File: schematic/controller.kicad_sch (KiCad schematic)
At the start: 2 parts, among them J5 Player 1, J7 Player 2

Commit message: bootup works, controller waits, but no response
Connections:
- net C2P4 is gone; now on net C4_ARM: J7.5
- net C2P7 is gone; now on net C7_FIRE: J7.8
- net C1P4 renamed C4_ARM
- net C1P7 renamed C7_FIRE
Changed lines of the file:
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@@
 (kicad_sch (version 20230121) (generator eeschema)
   (paper "A4")
-  (bus_entry (at 152.781 127.127) (size 2.54 2.54)
-    (stroke (width 0) (type default))
+  (junction (at 149.225 109.601) (diameter 0) (color 0 0 0 0)
+  )
+  (junction (at 151.13 112.649) (diameter 0) (color 0 0 0 0)
   )
   (bus_entry (at 152.781 84.709) (size 2.54 2.54)
@@
     (stroke (width 0) (type default))
   )
-  (bus_entry (at 152.781 134.747) (size 2.54 2.54)
-    (stroke (width 0) (type default))
-  )
   (bus_entry (at 152.781 124.587) (size 2.54 2.54)
     (stroke (width 0) (type default))
@@
     (stroke (width 0) (type default))
   )
-  (bus_entry (at 152.781 94.869) (size 2.54 2.54)
-    (stroke (width 0) (type default))
-  )
   (bus_entry (at 152.781 97.409) (size 2.54 2.54)
     (stroke (width 0) (type default))
@@
     (stroke (width 0) (type default))
   )
-  (bus_entry (at 152.781 102.489) (size 2.54 2.54)
-    (stroke (width 0) (type default))
-  )
   (bus_entry (at 152.781 132.207) (size 2.54 2.54)
     (stroke (width 0) (type default))
@@
     (stroke (width 0) (type default))
   )
-  (wire (pts (xy 141.859 127.127) (xy 152.781 127.127))
-    (stroke (width 0) (type default))
-  )
-  (wire (pts (xy 141.859 102.489) (xy 152.781 102.489))
+  (wire (pts (xy 141.859 102.489) (xy 151.13 102.489))
     (stroke (width 0) (type default))
   )
@@
     (stroke (width 0) (type default))
   )
+  (wire (pts (xy 141.859 127.127) (xy 149.225 127.127))
+    (stroke (width 0) (type default))
+  )
   (bus (pts (xy 155.321 87.249) (xy 155.321 89.789))
     (stroke (width 0) (type default))
@@
     (stroke (width 0) (type default))
   )
+  (wire (pts (xy 149.225 109.601) (xy 149.225 94.869))
+    (stroke (width 0) (type default))
+  )
   (bus (pts (xy 155.321 94.869) (xy 155.321 97.409))
     (stroke (width 0) (type default))
   )
-  (wire (pts (xy 141.859 134.747) (xy 152.781 134.747))
+  (wire (pts (xy 149.225 127.127) (xy 149.225 109.601))
     (stroke (width 0) (type default))
   )
@@
     (stroke (width 0) (type default))
   )
-  (bus (pts (xy 155.321 127.127) (xy 155.321 129.667))
+  (wire (pts (xy 151.13 102.489) (xy 151.13 112.649))
+    (stroke (width 0) (type default))
+  )
+  (wire (pts (xy 149.225 109.601) (xy 153.67 109.601))
     (stroke (width 0) (type default))
   )
@@
     (stroke (width 0) (type default))
   )
-  (wire (pts (xy 141.859 94.869) (xy 152.781 94.869))
+  (wire (pts (xy 151.13 112.649) (xy 151.13 134.747))
+    (stroke (width 0) (type default))
+  )
+  (wire (pts (xy 141.859 94.869) (xy 149.225 94.869))
     (stroke (width 0) (type default))
   )
@@
     (stroke (width 0) (type default))
   )
-  (bus (pts (xy 155.321 129.667) (xy 155.321 132.207))
+  (bus (pts (xy 155.321 127.127) (xy 155.321 132.207))
     (stroke (width 0) (type default))
   )
@@
     (stroke (width 0) (type default))
   )
+  (wire (pts (xy 141.859 134.747) (xy 151.13 134.747))
+    (stroke (width 0) (type default))
+  )
+  (wire (pts (xy 151.13 112.649) (xy 153.67 112.649))
+    (stroke (width 0) (type default))
+  )
   (label "C1P3" (at 141.986 97.409 0) (fields_autoplaced)
     (effects (font (size 1.27 1.27)) (justify left bottom))
@@
     (effects (font (size 1.27 1.27)) (justify left bottom))
   )
-  (label "C2P4" (at 141.986 134.747 0) (fields_autoplaced)
-    (effects (font (size 1.27 1.27)) (justify left bottom))
-  )
   (label "C1P0" (at 141.986 82.169 0) (fields_autoplaced)
     (effects (font (size 1.27 1.27)) (justify left bottom))
   )
-  (label "C1P4" (at 141.986 102.489 0) (fields_autoplaced)
-    (effects (font (size 1.27 1.27)) (justify left bottom))
-  )
   (label "C2P2" (at 141.986 124.587 0) (fields_autoplaced)
     (effects (font (size 1.27 1.27)) (justify left bottom))
@@
     (effects (font (size 1.27 1.27)) (justify left bottom))
   )
-  (label "C2P7" (at 142.113 127.127 0) (fields_autoplaced)
-    (effects (font (size 1.27 1.27)) (justify left bottom))
-  )
   (label "C1P5" (at 142.113 84.709 0) (fields_autoplaced)
     (effects (font (size 1.27 1.27)) (justify left bottom))
@@
     (effects (font (size 1.27 1.27)) (justify left bottom))
   )
-  (label "C1P7" (at 142.113 94.869 0) (fields_autoplaced)
-    (effects (font (size 1.27 1.27)) (justify left bottom))
-  )
   (label "C2P6" (at 142.113 122.047 0) (fields_autoplaced)
     (effects (font (size 1.27 1.27)) (justify left bottom))
@@
     (effects (font (size 1.27 1.27)) (justify left))
   )
+  (hierarchical_label "C7_FIRE" (shape input) (at 153.67 109.601 0) (fields_autoplaced)
+    (effects (font (size 1.27 1.27)) (justify left))
+  )
   (hierarchical_label "C1P[0..8]" (shape bidirectional) (at 159.766 105.029 0) (fields_autoplaced)
     (effects (font (size 1.27 1.27)) (justify left))
   )
+  (hierarchical_label "C4_ARM" (shape input) (at 153.67 112.649 0) (fields_autoplaced)
+    (effects (font (size 1.27 1.27)) (justify left))
+  )

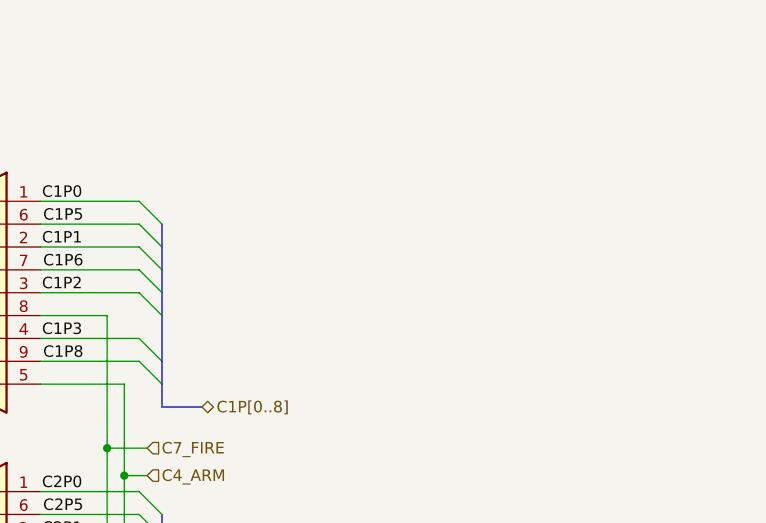
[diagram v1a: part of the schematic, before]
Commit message: added volume and adjusted cart port
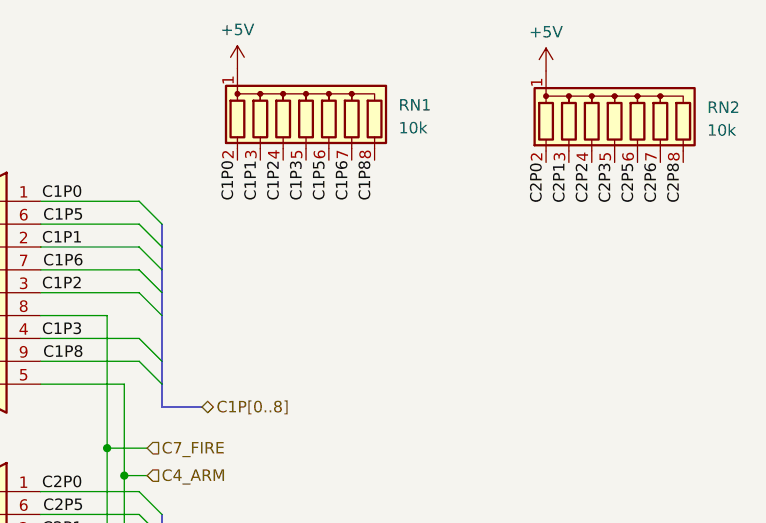
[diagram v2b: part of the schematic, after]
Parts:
- added RN1, RN2: 10k, Resistor_THT:R_Array_SIP8, symbol Device:R_Network07
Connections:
- net C1P0: now also RN1.2 (R1)
- net C1P1: now also RN1.3 (R2)
- net C1P2: now also RN1.4 (R3)
- net C1P3: now also RN1.5 (R4)
- net C1P5: now also RN1.6 (R5)
- net C1P6: now also RN1.7 (R6)
- net C1P8: now also RN1.8 (R7)
- net C2P0: now also RN2.2 (R1)
- net C2P1: now also RN2.3 (R2)
- net C2P2: now also RN2.4 (R3)
- net C2P3: now also RN2.5 (R4)
- net C2P5: now also RN2.6 (R5)
- net C2P6: now also RN2.7 (R6)
- net C2P8: now also RN2.8 (R7)
- new net +5V: RN1.1 (common), RN2.1 (common)
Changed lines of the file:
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@@
     (stroke (width 0) (type default))
   )
-  (bus (pts (xy 155.321 97.409) (xy 155.321 99.949))
+  (bus (pts (xy 155.321 94.869) (xy 155.321 99.949))
     (stroke (width 0) (type default))
   )
@@
     (stroke (width 0) (type default))
   )
-  (bus (pts (xy 155.321 94.869) (xy 155.321 97.409))
-    (stroke (width 0) (type default))
-  )
   (wire (pts (xy 149.225 127.127) (xy 149.225 109.601))
     (stroke (width 0) (type default))
@@
     (stroke (width 0) (type default))
   )
+  (label "C2P0" (at 197.993 77.851 270) (fields_autoplaced)
+    (effects (font (size 1.27 1.27)) (justify right bottom))
+  )
   (label "C1P3" (at 141.986 97.409 0) (fields_autoplaced)
     (effects (font (size 1.27 1.27)) (justify left bottom))
@@
     (effects (font (size 1.27 1.27)) (justify left bottom))
   )
+  (label "C2P2" (at 203.073 77.851 270) (fields_autoplaced)
+    (effects (font (size 1.27 1.27)) (justify right bottom))
+  )
   (label "C2P0" (at 141.986 114.427 0) (fields_autoplaced)
     (effects (font (size 1.27 1.27)) (justify left bottom))
   )
+  (label "C2P3" (at 205.613 77.851 270) (fields_autoplaced)
+    (effects (font (size 1.27 1.27)) (justify right bottom))
+  )
+  (label "C1P2" (at 168.783 77.597 270) (fields_autoplaced)
+    (effects (font (size 1.27 1.27)) (justify right bottom))
+  )
   (label "C1P1" (at 141.986 87.249 0) (fields_autoplaced)
     (effects (font (size 1.27 1.27)) (justify left bottom))
@@
     (effects (font (size 1.27 1.27)) (justify left bottom))
   )
+  (label "C1P8" (at 178.943 77.597 270) (fields_autoplaced)
+    (effects (font (size 1.27 1.27)) (justify right bottom))
+  )
   (label "C2P2" (at 141.986 124.587 0) (fields_autoplaced)
     (effects (font (size 1.27 1.27)) (justify left bottom))
   )
+  (label "C2P8" (at 213.233 77.851 270) (fields_autoplaced)
+    (effects (font (size 1.27 1.27)) (justify right bottom))
+  )
+  (label "C1P0" (at 163.703 77.597 270) (fields_autoplaced)
+    (effects (font (size 1.27 1.27)) (justify right bottom))
+  )
+  (label "C2P1" (at 200.533 77.851 270) (fields_autoplaced)
+    (effects (font (size 1.27 1.27)) (justify right bottom))
+  )
   (label "C2P3" (at 141.986 129.667 0) (fields_autoplaced)
     (effects (font (size 1.27 1.27)) (justify left bottom))
@@
     (effects (font (size 1.27 1.27)) (justify left bottom))
   )
+  (label "C1P1" (at 166.243 77.597 270) (fields_autoplaced)
+    (effects (font (size 1.27 1.27)) (justify right bottom))
+  )
   (label "C2P6" (at 142.113 122.047 0) (fields_autoplaced)
     (effects (font (size 1.27 1.27)) (justify left bottom))
@@
   (label "C2P5" (at 142.113 116.967 0) (fields_autoplaced)
     (effects (font (size 1.27 1.27)) (justify left bottom))
+  )
+  (label "C2P5" (at 208.153 77.851 270) (fields_autoplaced)
+    (effects (font (size 1.27 1.27)) (justify right bottom))
+  )
+  (label "C1P6" (at 176.403 77.597 270) (fields_autoplaced)
+    (effects (font (size 1.27 1.27)) (justify right bottom))
+  )
+  (label "C1P5" (at 173.863 77.597 270) (fields_autoplaced)
+    (effects (font (size 1.27 1.27)) (justify right bottom))
+  )
+  (label "C2P6" (at 210.693 77.851 270) (fields_autoplaced)
+    (effects (font (size 1.27 1.27)) (justify right bottom))
+  )
+  (label "C1P3" (at 171.323 77.597 270) (fields_autoplaced)
+    (effects (font (size 1.27 1.27)) (justify right bottom))
   )
   (hierarchical_label "C2P[0..8]" (shape bidirectional) (at 159.766 137.287 0) (fields_autoplaced)
@@
     )
   )
+  (symbol (lib_id "power:+5V") (at 163.703 67.437 0) (unit 1)
+    (in_bom yes) (on_board yes) (dnp no) (fields_autoplaced)
+    (property "Reference" "#PWR061" (at 163.703 71.247 0)
+      (effects (font (size 1.27 1.27)) hide)
+    )
+    (property "Value" "+5V" (at 163.703 63.119 0)
+      (effects (font (size 1.27 1.27)))
+    )
+    (property "Footprint" "" (at 163.703 67.437 0)
+      (effects (font (size 1.27 1.27)) hide)
+    )
+    (property "Datasheet" "" (at 163.703 67.437 0)
+      (effects (font (size 1.27 1.27)) hide)
+    )
+    (pin "1")
+    (instances
+      (project "coleco_original"
+        (path "/970e0f64-111f-41e3-9f5a-fb0d0f6fa101/3558c718-2222-493c-b2cb-6973deed0f63"
+          (reference "#PWR061") (unit 1)
+        )
+        (path "/970e0f64-111f-41e3-9f5a-fb0d0f6fa101/ebfedf81-c577-48d2-9dda-bc832656750a"
+          (reference "#PWR078") (unit 1)
+        )
+      )
+    )
+  )
+  (symbol (lib_id "Device:R_Network07") (at 205.613 72.771 0) (unit 1)
+    (in_bom yes) (on_board yes) (dnp no) (fields_autoplaced)
+    (property "Reference" "RN2" (at 215.9 71.755 0)
+      (effects (font (size 1.27 1.27)) (justify left))
+    )
+    (property "Value" "10k" (at 215.9 74.295 0)
+      (effects (font (size 1.27 1.27)) (justify left))
+    )
+    (property "Footprint" "Resistor_THT:R_Array_SIP8" (at 217.678 72.771 90)
+      (effects (font (size 1.27 1.27)) hide)
+    )
+    (property "Datasheet" "http://www.vishay.com/docs/31509/csc.pdf" (at 205.613 72.771 0)
+      (effects (font (size 1.27 1.27)) hide)
+    )
+    (pin "7")
+    (pin "4")
+    (pin "5")
+    (pin "1")
+    (pin "3")
+    (pin "8")
+    (pin "6")
+    (pin "2")
+    (instances
+      (project "coleco_original"
+        (path "/970e0f64-111f-41e3-9f5a-fb0d0f6fa101/ebfedf81-c577-48d2-9dda-bc832656750a"
+          (reference "RN2") (unit 1)
+        )
+      )
+    )
+  )
+  (symbol (lib_id "Device:R_Network07") (at 171.323 72.517 0) (unit 1)
+    (in_bom yes) (on_board yes) (dnp no) (fields_autoplaced)
+    (property "Reference" "RN1" (at 181.61 71.501 0)
+      (effects (font (size 1.27 1.27)) (justify left))
+    )
+    (property "Value" "10k" (at 181.61 74.041 0)
+      (effects (font (size 1.27 1.27)) (justify left))
+    )
+    (property "Footprint" "Resistor_THT:R_Array_SIP8" (at 183.388 72.517 90)
+      (effects (font (size 1.27 1.27)) hide)
+    )
+    (property "Datasheet" "http://www.vishay.com/docs/31509/csc.pdf" (at 171.323 72.517 0)
+      (effects (font (size 1.27 1.27)) hide)
+    )
+    (pin "7")
+    (pin "4")
+    (pin "5")
+    (pin "1")
+    (pin "3")
+    (pin "8")
+    (pin "6")
+    (pin "2")
+    (instances
+      (project "coleco_original"
+        (path "/970e0f64-111f-41e3-9f5a-fb0d0f6fa101/ebfedf81-c577-48d2-9dda-bc832656750a"
+          (reference "RN1") (unit 1)
+        )
+      )
+    )
+  )
   (symbol (lib_id "Connector:DB9_Male") (at 134.239 92.329 180) (unit 1)
     (in_bom yes) (on_board yes) (dnp no)
@@
         )
       )
+    )
+  )
+  (symbol (lib_id "power:+5V") (at 197.993 67.691 0) (unit 1)
+    (in_bom yes) (on_board yes) (dnp no) (fields_autoplaced)
+    (property "Reference" "#PWR061" (at 197.993 71.501 0)
+      (effects (font (size 1.27 1.27)) hide)
+    )
+    (property "Value" "+5V" (at 197.993 63.373 0)
+      (effects (font (size 1.27 1.27)))
+    )
+    (property "Footprint" "" (at 197.993 67.691 0)
+      (effects (font (size 1.27 1.27)) hide)
+    )
+    (property "Datasheet" "" (at 197.993 67.691 0)
+      (effects (font (size 1.27 1.27)) hide)
+    )
+    (pin "1")
+    (instances
+      (project "coleco_original"
+        (path "/970e0f64-111f-41e3-9f5a-fb0d0f6fa101/3558c718-2222-493c-b2cb-6973deed0f63"
+          (reference "#PWR061") (unit 1)
+        )
+        (path "/970e0f64-111f-41e3-9f5a-fb0d0f6fa101/ebfedf81-c577-48d2-9dda-bc832656750a"
+          (reference "#PWR079") (unit 1)
+        )
+      )

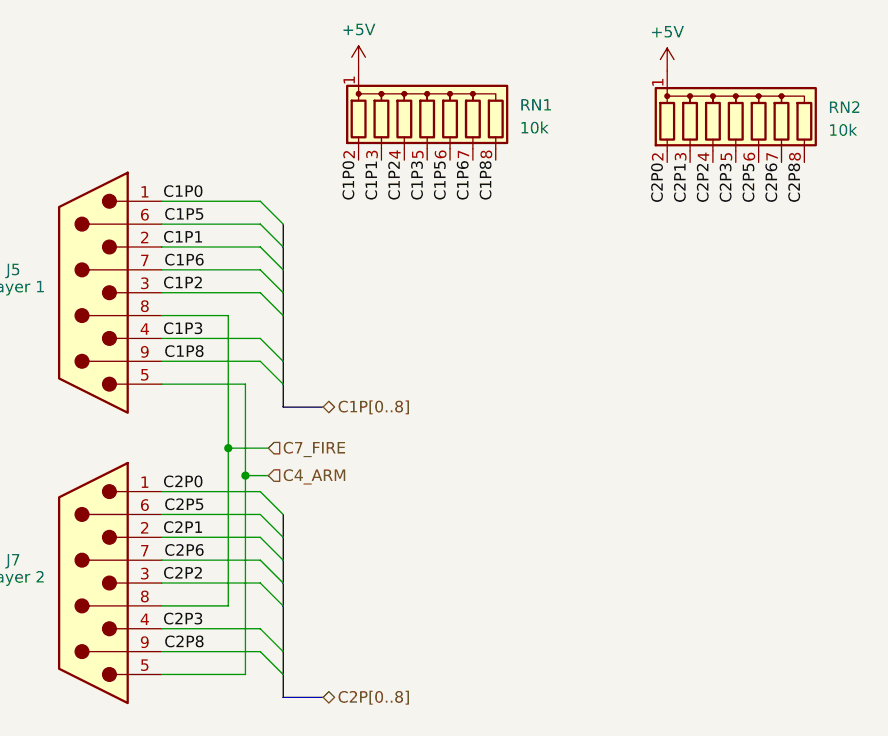
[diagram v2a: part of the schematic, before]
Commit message: first version with roller controller compat
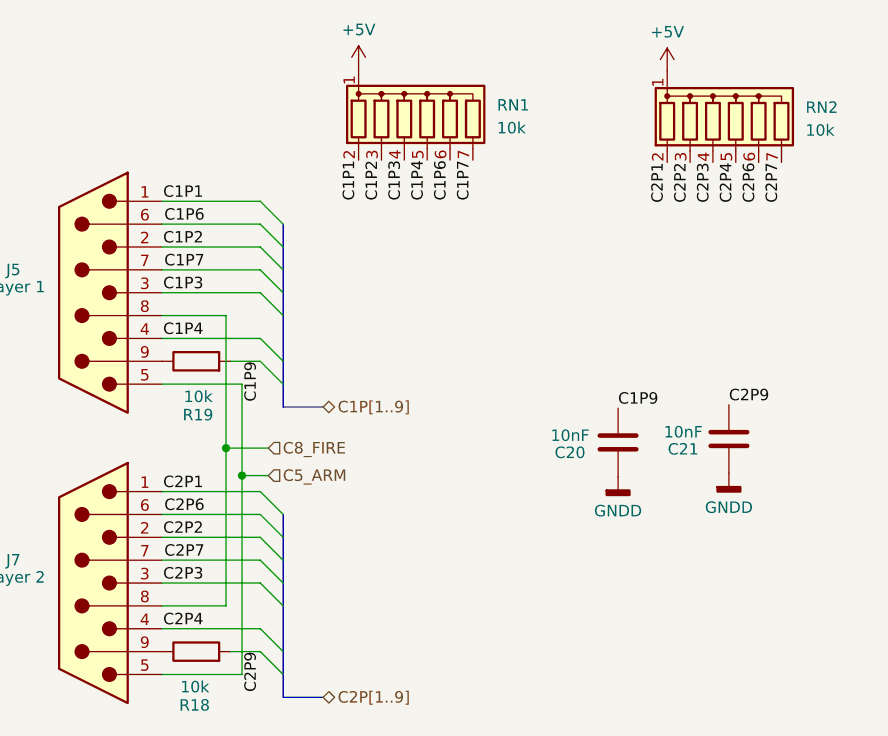
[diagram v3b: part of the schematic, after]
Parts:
- added C20, C21: 10nF, Capacitor_THT:C_Disc_D7.0mm_W2.5mm_P5.00mm, symbol Device:C
- added R18, R19: 10k, Resistor_THT:R_Axial_DIN0207_L6.3mm_D2.5mm_P10.16mm_Horizontal, symbol Device:R
- RN1, RN2: footprint Resistor_THT:R_Array_SIP8 -> Resistor_THT:R_Array_SIP7; symbol Device:R_Network07 -> Device:R_Network06
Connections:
- net C1P0 is gone; now on net C1P1: J5.1, RN1.2 (R1)
- net C1P5 is gone; now on net C1P6: J5.6, RN1.6 (R5)
- net C2P0 is gone; now on net C2P1: J7.1, RN2.2 (R1)
- net C2P5 is gone; now on net C2P6: J7.6, RN2.6 (R5)
- net C1P1: no longer J5.2, RN1.3 (R2)
- net C1P2: now also J5.2, RN1.3 (R2); no longer J5.3, RN1.4 (R3)
- net C1P3: now also J5.3, RN1.4 (R3); no longer J5.4, RN1.5 (R4)
- net C1P6: no longer J5.7, RN1.7 (R6)
- net C2P1: no longer J7.2, RN2.3 (R2)
- net C2P2: now also J7.2, RN2.3 (R2); no longer J7.3, RN2.4 (R3)
- net C2P3: now also J7.3, RN2.4 (R3); no longer J7.4, RN2.5 (R4)
- net C2P6: no longer J7.7, RN2.7 (R6)
- net C1P8: no longer names the net of J5.9
- net C1P8: now also R19.1; no longer RN1.8 (R7)
- net C2P8: no longer names the net of J7.9
- net C2P8: now also R18.1; no longer RN2.8 (R7)
- net C4_ARM renamed C5_ARM
- net C7_FIRE renamed C8_FIRE
- new net C1P4: J5.4, RN1.5 (R4)
- new net C1P7: J5.7, RN1.7 (R6)
- new net C1P9: C20.1, R19.2
- new net C2P4: J7.4, RN2.5 (R4)
- new net C2P7: J7.7, RN2.7 (R6)
- new net C2P9: C21.1, R18.2
- new net GNDD: C20.2, C21.2

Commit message: update pdf schematic and schematic wording
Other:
- company: (none) -> sparkletron
- title: (none) -> Mini Colecovision
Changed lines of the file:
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@@
 (kicad_sch (version 20230121) (generator eeschema)
-  (paper "A4")
+  (paper "USLetter")
+  (title_block
+    (title "Mini Colecovision")
+    (date "2024-03-25")
+    (rev "1.0.0")
+    (company "sparkletron")
+    (comment 1 "Jay Convertino")
+    (comment 2 "MIT LICENSE")
+    (comment 3 "TARGET: Portable")
+  )
   (junction (at 150.749 112.649) (diameter 0) (color 0 0 0 0)
   )
